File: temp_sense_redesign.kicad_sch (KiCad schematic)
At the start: 105 parts, among them IC1 TLV75533PDYDR, J1 Screw_Terminal_01x08, J2 Screw_Terminal_01x08, J3 Screw_Terminal_01x08, SW1 SW_Push, U2 AP63205, U3 MCP2517FDT-H_SL, U5 CLV4051ATDWRG4Q1, U6 CLV4051ATDWRG4Q1, U7 CLV4051ATDWRG4Q1, Y1 Crystal

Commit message: main
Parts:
- added C41: 1uF, Capacitor_SMD:C_1206_3216Metric_Pad1.33x1.80mm_HandSolder, symbol Device:C
- added C42: 1u, Capacitor_SMD:C_1206_3216Metric_Pad1.33x1.80mm_HandSolder, symbol Device:C
- added D1: Littelfuse SMF24CA, Diode_SMD:D_SOD-123F, symbol Device:D_TVS_Small
- added F1: Fuse, symbol Device:Fuse
- added IC2: LM74500QDDFRQ1, SOT65P280X110-8N, symbol custom_components:LM74500QDDFRQ1
- added J4: Conn_01x02_Pin, symbol Connector:Conn_01x02_Pin
- added J6: Screw_Terminal_01x08, symbol Connector:Screw_Terminal_01x08
- added Q1: Q_NMOS_DGS, symbol Transistor_FET:Q_NMOS_DGS
- added TP1, TP2, TP3: TestPoint, symbol Connector:TestPoint
- IC1: value TLV75533PDYDR -> TPS7A03
- U1: value ~ -> MSPM0C1104SDGS20R
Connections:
- net +3.3V: now also TP1.1
- net +5V: now also TP2.1
- net GND: now also J1.4 (Pin_4), J1.8 (Pin_8), J2.4 (Pin_4), J2.8 (Pin_8), J3.4 (Pin_4), J3.8 (Pin_8), J6.4 (Pin_4), J6.8 (Pin_8), TP3.1
- net SWCLK: now also J4.1 (Pin_1)
- net TI12: now also J6.3 (Pin_3); no longer J2.4 (Pin_4)
- net TI16: now also J6.5 (Pin_5); no longer J2.8 (Pin_8)
- net TI20: now also J6.6 (Pin_6); no longer J3.4 (Pin_4)
- net TI24: now also J6.7 (Pin_7); no longer J3.8 (Pin_8)
- net TI4: now also J6.1 (Pin_1); no longer J1.4 (Pin_4)
- net TI8: now also J6.2 (Pin_2); no longer J1.8 (Pin_8)
- net at U1.15 (PA19/SWDIO): now also J4.2 (Pin_2)
- net +12V renamed 24V
- net 24V: now also F1.2, Q1.1 (D)
- net AI4: no longer names the net of U1.12 (PA16/A8)
- net AI5: no longer names the net of U1.1 (PA26/A1)
- net UART_RX: no longer names the net of U1.3 (PA28/A5)
- net UART_TX: no longer names the net of U1.2 (PA27/A0)
- new net: C42.1, D1.2 (A2), IC2.1 (EN), Q1.3 (S)
- new net: C42.2, D1.1 (A1), IC2.2 (GND)
- new net: C41.1, IC2.4 (VCAP)
- new net: C41.2, F1.1, IC2.5 (SOURCE)
- new net gate: IC2.6 (GATE), Q1.2 (G)
- no-connect marks 3 -> 7

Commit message: final
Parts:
- removed R2: 120, symbol Device:R_Small
- removed R27, R28, R29, R30, R35, R36, R39, R40, R43, R44, R45, R46: 1M, Resistor_SMD:R_0603_1608Metric, symbol Device:R_Small
- removed R31, R32, R33, R34, R37, R38, R41, R42, R47, R48, R49, R50: 680, Resistor_SMD:R_0603_1608Metric, symbol Device:R_Small
- added C43: 1uF, Capacitor_SMD:C_0603_1608Metric, symbol Device:C_Small
- added J5: Screw_Terminal_01x02, symbol Connector:Screw_Terminal_01x02
- added J7: Conn_01x02_Pin, symbol Connector:Conn_01x02_Pin
- added R81: 1M, Resistor_SMD:R_0603_1608Metric, symbol Device:R_Small
- R10, R13, R14, R17, R18, R19, R23, R24, R3, R5, R6, R9: value 1M -> 680
- Y1: value Crystal -> HC49/4HSMX
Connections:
- net +3.3V: no longer R11.2, R12.2, R15.2, R16.2, R20.2, R21.2, R22.2, R25.2, R26.2, R4.2, R7.2, R8.2
- net +5V: now also C14.1, IC1.3 (EN)
- net 24V: no longer C1.1, U2.2 (EN), U2.3 (VIN)
- net CANL: now also J5.2 (Pin_2)
- net GND: now also C43.2, J7.2 (Pin_2)
- net T1: now also R21.1; no longer R17.2
- net T10: now also R11.1; no longer R19.2
- net T11: now also R12.1; no longer R23.2
- net T12: now also R13.1; no longer R24.2
- net T13: now also R14.1
- net T14: now also R15.1
- net T15: now also R16.1
- net T16: now also R17.1
- net T17: now also R18.1
- net T18: now also R19.1
- net T19: now also R20.1
- net T2: now also R3.1; no longer R3.2
- net T20: now also R22.1
- net T21: now also R23.1
- net T22: now also R24.1
- net T23: now also R25.1
- net T24: now also R26.1
- net T3: now also R4.1; no longer R5.2
- net T4: now also R5.1; no longer R6.2
- net T5: now also R6.1; no longer R9.2
- net T6: now also C23.1, R7.1, R7.2; no longer C22.1, R10.2
- net T7: now also C25.1, R9.1; no longer C23.1, R13.2
- net T8: now also R8.1; no longer R14.2
- net T9: now also C22.1, R10.1; no longer C25.1, R18.2
- net TI1: now also R21.2; no longer R17.1, R21.1
- net TI10: now also R11.2; no longer R19.1, R22.1
- net TI11: now also R12.2; no longer R23.1, R25.1
- net TI12: now also R13.2; no longer R24.1, R26.1
- net TI13: now also R14.2
- net TI14: now also R15.2
- net TI15: now also R16.2
- net TI16: now also R17.2
- net TI17: now also R18.2
- net TI18: now also R19.2
- net TI19: now also R20.2
- net TI2: now also R3.2; no longer R3.1, R4.1
- net TI20: now also R22.2
- net TI21: now also R23.2
- net TI22: now also R24.2
- net TI23: now also R25.2
- net TI24: now also R26.2
- net TI3: now also R4.2; no longer R5.1, R7.1
- net TI4: now also R5.2; no longer R6.1, R8.1
- net TI5: now also R6.2; no longer R11.1, R9.1
- net TI6: no longer R10.1, R12.1
- net TI7: now also R9.2; no longer R13.1, R15.1
- net TI8: now also R8.2; no longer R14.1, R16.1
- net TI9: now also R10.2; no longer R18.1, R20.1
- net at U1.1 (PA26/A1): now also R81.1
- net CAN_H renamed CANH
- net CANH: now also J5.1 (Pin_1)
- new net +24V: C1.1, U2.2 (EN), U2.3 (VIN)
- new net AOUT: C43.1, J7.1 (Pin_1), R81.2
- no-connect marks 7 -> 6
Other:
- moved on the sheet: C10, C11, C12, C14, C17, C41, C42, C8, C9, D1, F1, IC2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

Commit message: Update design files, add custom library and footprints
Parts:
- removed C10, C11: 22p, Capacitor_SMD:C_1206_3216Metric_Pad1.33x1.80mm_HandSolder, symbol Device:C
- removed C12: 0.1uF, Capacitor_SMD:C_1206_3216Metric_Pad1.33x1.80mm_HandSolder, symbol Device:C
- removed C14, C15, C41: 1uF, Capacitor_SMD:C_1206_3216Metric_Pad1.33x1.80mm_HandSolder, symbol Device:C
- removed C42: 1u, Capacitor_SMD:C_1206_3216Metric_Pad1.33x1.80mm_HandSolder, symbol Device:C
- removed C8, C9: 0.1µ, Capacitor_SMD:C_1206_3216Metric_Pad1.33x1.80mm_HandSolder, symbol Device:C
- removed R26: 680, Resistor_SMD:R_0603_1608Metric, symbol Device:R_Small
- added C10: 22p, Capacitor_SMD:C_0603_1608Metric, symbol Device:C_Small
- added C11: 10u, Capacitor_SMD:C_0603_1608Metric_Pad1.08x0.95mm_HandSolder, symbol Device:C_Small
- added C12, C8, C9: 0.1µF, Capacitor_SMD:C_0603_1608Metric, symbol Device:C_Small
- added C14, C15, C41, C42: 1uF, Capacitor_SMD:C_0603_1608Metric, symbol Device:C_Small
- added H1, H2, H3, H4: MountingHole, MountingHole:MountingHole_3.2mm_M3, symbol Mechanical:MountingHole
- added J8: Screw_Terminal_01x02, Library:1725656, symbol Connector:Screw_Terminal_01x02
- added R2: 680, Resistor_SMD:R_0603_1608Metric, symbol Device:R_Small
- C1: value 10μ -> 22uF; footprint (none) -> Capacitor_SMD:C_0603_1608Metric; Inventory (none) -> No; Mouser P/N (none) -> 963-MLASG32MSB5226MP
- C13, C16: value 1uF -> 0.1µF; Inventory (none) -> Yes; Mouser P/N (none) -> 81-GCM188R71C104KA7J
- C17, C18, C19, C20, C21, C22, C23, C24, C25, C26, C27, C28, C29, C30, C31, C32, C33, C34, C35, C36, C37, C38, C39: Inventory (none) -> No; Mouser P/N (none) -> 81-GXT155R61A474KE1D
- C2: footprint (none) -> Capacitor_SMD:C_0603_1608Metric; Mouser P/N (none) -> 810-C1608X8R1H104K
- C3: value 22μ -> 22uF; footprint (none) -> Capacitor_SMD:C_0603_1608Metric; Inventory (none) -> No; Mouser P/N (none) -> 963-MLASG32MSB5226MP
- C4: value 22μ -> 10u; footprint (none) -> Capacitor_SMD:C_0603_1608Metric; Inventory (none) -> No; Mouser P/N (none) -> 81-ZRB18AR6YA106ME1L
- C40: value 470nF -> 0.1µF; Inventory (none) -> Yes; Mouser P/N (none) -> 81-GCM188R71C104KA7J
- C43: Inventory (none) -> Yes; Mouser P/N (none) -> 81-GRM1887R1E105KA2D
- C44: value 1uF -> 22p; Inventory (none) -> No; Mouser P/N (none) -> 81-GCQ0335C1H220JB1D
- C5: value 10µ -> 470nF; footprint (none) -> Capacitor_SMD:C_0603_1608Metric; Inventory (none) -> No; Mouser P/N (none) -> 81-GXT155R61A474KE1D
- C6: value 0.1µ -> 0.1µF; footprint (none) -> Capacitor_SMD:C_0603_1608Metric; Inventory (none) -> Yes; Mouser P/N (none) -> 81-GCM188R71C104KA7J
- C7: value 100µ -> 10n; footprint (none) -> Capacitor_SMD:C_0603_1608Metric; Inventory (none) -> Yes; Mouser P/N (none) -> 603-CC0603JR7R7BB103
- D1: Inventory (none) -> No; Mouser P/N (none) -> 576-SMF24CA
- F1: value Fuse -> 3568; footprint (none) -> Fuse:Fuseholder_Blade_Mini_Keystone_3568; Inventory (none) -> Yes; Mouser P/N (none) -> 534-3568
- IC2: footprint SOT65P280X110-8N -> Package_TO_SOT_SMD:TSOT-23-8_HandSoldering; Arrow Part Number LM74500QDDFRQ1 -> (none); Arrow Price/Stock null?region=nac -> (none); Height 1.1 -> (none); Manufacturer_Name Texas Instruments -> (none); Manufacturer_Part_Number LM74500QDDFRQ1 -> (none); Mouser P/N (none) -> 595-LM74500QDDFRQ1; Mouser Part Number 595-LM74500QDDFRQ1 -> (none); Mouser Price/Stock https://www.mouser.co.uk/ProductDetail/Texas-Instruments/LM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 -> (none)
- J1, J2, J3, J6: footprint (none) -> Library:1725711; Inventory (none) -> No; Mouser P/N (none) -> 490-TB003-500-P03BE
- J4, J7: footprint (none) -> Connector_PinSocket_2.00mm:PinSocket_1x02_P2.00mm_Vertical
- J5: footprint (none) -> Library:1725656; Inventory (none) -> No; Mouser P/N (none) -> 651-1725656
- L1: footprint (none) -> Library:inductorcustome27; Inventory (none) -> No; Mouser P/N (none) -> 70-IHLP2020BZR4R7M1A
- Q1: value Q_NMOS_DGS -> SUD20N10-66L-GE3; footprint (none) -> Library:SUD20N1066LGE3; Inventory (none) -> No; Mouser P/N (none) -> 78-SUD20N10-66L-GE3
- R1: footprint (none) -> Resistor_SMD:R_0603_1608Metric; Inventory (none) -> No; Mouser P/N (none) -> 652-CR1206FX-4752ELF
- R10, R11, R12, R13, R14, R15, R16, R17, R18, R19, R20, R21, R22, R23, R24, R25, R3, R4, R5, R6, R7, R8, R9: Inventory (none) -> Yes; Mouser P/N (none) -> 667-ERJ-3EKF6800V
- R81: Inventory (none) -> Yes; Mouser P/N (none) -> 667-ERJ-3EKF1004V
- SW1: footprint (none) -> Library:KSC251JSPDELTALFS; Inventory (none) -> No; Mouser P/N (none) -> 611-KSC251JSPDELTALF
- TP1, TP2, TP3: footprint (none) -> TestPoint:TestPoint_Pad_1.5x1.5mm
- U1: footprint (none) -> Library:MSPMOC; Mouser P/N (none) -> 595-MSPM0C1104SDG20R
- U2: Inventory (none) -> No; Mouser P/N (none) -> 621-AP63205WU-7
- U3: footprint (none) -> Package_SO:SOIC-14_3.9x8.7mm_P1.27mm; Mouser P/N (none) -> 579-MCP2517FD-H/SL
- U4: value ~ -> MCP2517FD-H/SL; footprint (none) -> Package_TO_SOT_SMD:Texas_DDF0008A_SOT-8_1.6x2.9mm_P0.65mm; Mouser P/N (none) -> 595-TCAN1057AVDDFRQ1
- U5, U6, U7: Mouser P/N (none) -> 595-CLV4051ATDWRG4Q1
- Y1: footprint (none) -> Library:830017146; Inventory (none) -> No; Mouser P/N (none) -> 710-830017146
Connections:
- net +3.3V: now also C13.2, C16.2, C4.1, C40.2, C6.2, R1.2, U1.6 (VDD), U4.5 (VIO), C12.1, C15.1, C8.2; no longer C13.1, C16.1, C44.1, U4.8 (VIO)
- net +5V: now also C1.1, C14.2, C9.2; no longer C4.1
- net AI2: no longer U7.3 (X)
- net AI3: now also U7.3 (X)
- net CANH: now also J5.2 (Pin_2), U4.7 (CANH); no longer J5.1 (Pin_1), U4.6 (CANH)
- net CANL: now also J5.1 (Pin_1), U4.6 (CANL); no longer J5.2 (Pin_2), U4.7 (CANL)
- net GND: now also C13.1, C16.1, C40.1, C44.1, C5.2, J3.1 (Pin_1), J3.5 (Pin_5), J6.1 (Pin_1), J6.5 (Pin_5), U4.8 (S), C10.1, C11.1, C12.2, C14.1, C15.2, C8.1, C9.1, J8.2 (Pin_2); no longer C13.2, C16.2, C40.2, C44.2, C5.1, J3.4 (Pin_4), J3.8 (Pin_8), J6.4 (Pin_4), J6.8 (Pin_8), U4.5 (S)
- net T16: now also R9.1; no longer R17.1
- net T17: now also C22.1, R17.1; no longer C33.1, R18.1
- net T18: now also C33.1, R18.1; no longer C34.1, R19.1
- net T19: now also C34.1, R19.1; no longer C35.1, R20.1
- net T2: now also R2.1; no longer R3.1
- net T20: now also C35.1, R20.1; no longer C36.1, R22.1
- net T21: now also C36.1, R22.1; no longer C37.1, R23.1
- net T22: now also C37.1, R23.1; no longer C38.1, R24.1
- net T23: now also C38.1, R24.1; no longer C39.1, R25.1
- net T24: now also C39.1, R25.1; no longer C40.1
- net T3: now also R3.1; no longer R4.1
- net T4: now also R4.1; no longer R5.1
- net T5: now also R5.1; no longer R6.1
- net T6: now also R6.1; no longer R7.1, R7.2
- net T7: now also R8.1; no longer R9.1
- net T8: now also R7.1; no longer R8.1
- net T9: now also C5.1; no longer C22.1
- net TI1: now also J3.6 (Pin_6); no longer J1.1 (Pin_1)
- net TI10: now also J3.2 (Pin_2); no longer J2.2 (Pin_2)
- net TI11: now also J3.3 (Pin_3); no longer J2.3 (Pin_3)
- net TI12: now also J6.7 (Pin_7); no longer J6.3 (Pin_3)
- net TI13: now also J1.6 (Pin_6); no longer J2.5 (Pin_5)
- net TI14: now also J2.2 (Pin_2); no longer J2.6 (Pin_6)
- net TI15: now also J1.7 (Pin_7); no longer J2.7 (Pin_7)
- net TI16: now also J2.1 (Pin_1), R9.2; no longer J6.5 (Pin_5), R17.2
- net TI17: now also J6.3 (Pin_3), R17.2; no longer J3.1 (Pin_1), R18.2
- net TI18: now also J6.4 (Pin_4), R18.2; no longer J3.2 (Pin_2), R19.2
- net TI19: now also J6.6 (Pin_6), R19.2; no longer J3.3 (Pin_3), R20.2
- net TI2: now also J3.7 (Pin_7), R2.2; no longer J1.2 (Pin_2), R3.2
- net TI20: now also J6.2 (Pin_2), R20.2; no longer J6.6 (Pin_6), R22.2
- net TI21: now also J2.3 (Pin_3), R22.2; no longer J3.5 (Pin_5), R23.2
- net TI22: now also J2.7 (Pin_7), R23.2; no longer J3.6 (Pin_6), R24.2
- net TI23: now also J2.5 (Pin_5), R24.2; no longer J3.7 (Pin_7), R25.2
- net TI24: now also J2.6 (Pin_6), R25.2; no longer J6.7 (Pin_7)
- net TI3: now also J3.8 (Pin_8), R3.2; no longer J1.3 (Pin_3), R4.2
- net TI4: now also J3.4 (Pin_4), R4.2; no longer J6.1 (Pin_1), R5.2
- net TI5: now also J1.1 (Pin_1), R5.2; no longer J1.5 (Pin_5), R6.2
- net TI6: now also J1.5 (Pin_5), R6.2; no longer J1.6 (Pin_6)
- net TI7: now also J1.2 (Pin_2), R8.2; no longer J1.7 (Pin_7), R9.2
- net TI8: now also J1.3 (Pin_3), R7.2; no longer J6.2 (Pin_2), R8.2
- net TI9: now also J6.8 (Pin_8); no longer J2.1 (Pin_1)
- net at U3.6 (OSC1), Y1.1: now also C44.2
- net 24_bat: now reaches D1.2 (A2), IC2.1 (EN), Q1.3 (S)
- net 24_bat: now also F1.1, IC2.5 (SOURCE), C41.2, C42.1
- net at D1.1 (A1), IC2.2 (GND): now also C42.2
- net at IC2.4 (VCAP): now also C41.1
- net SWDIO: now reaches J4.2 (Pin_2), U1.15 (PA19/SWDIO)
- net at U3.5 (OSC2), Y1.2: now also C10.2
- net +24V renamed vbat_output
- net vbat_output: now also Q1.1 (D), C11.2; no longer C1.1
- removed net +3V3: C5.2, C6.2, R1.2, U1.6 (VDD)
- net 24V: no longer names the net of F1.2
- net 24V: now also J8.1 (Pin_1); no longer Q1.1 (D)
- no-connect marks 6 -> 9
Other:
- moved on the sheet: D1, F1, IC2, J1, J4, J5, J7, Q1, TP1, TP2, TP3, U3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

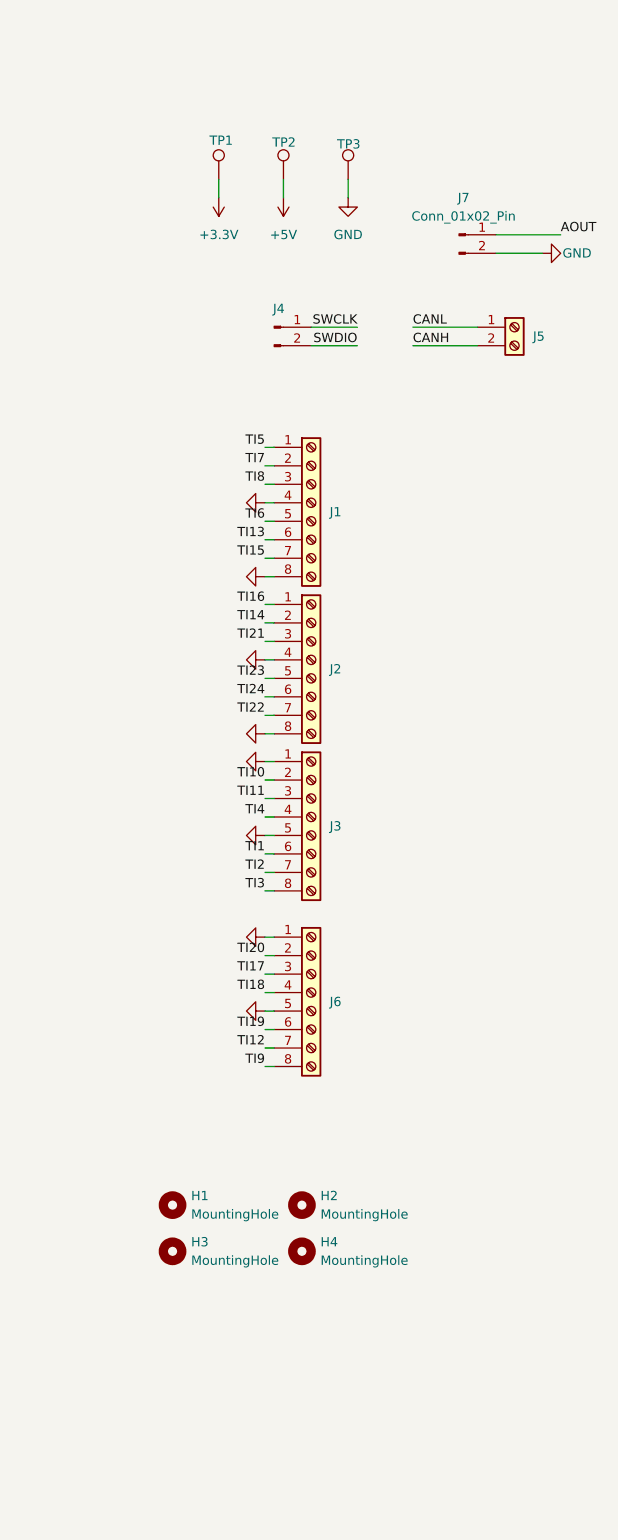
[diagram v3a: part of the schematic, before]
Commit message: Add KiCad .gitignore, remove gerber/backup/cache files from tracking
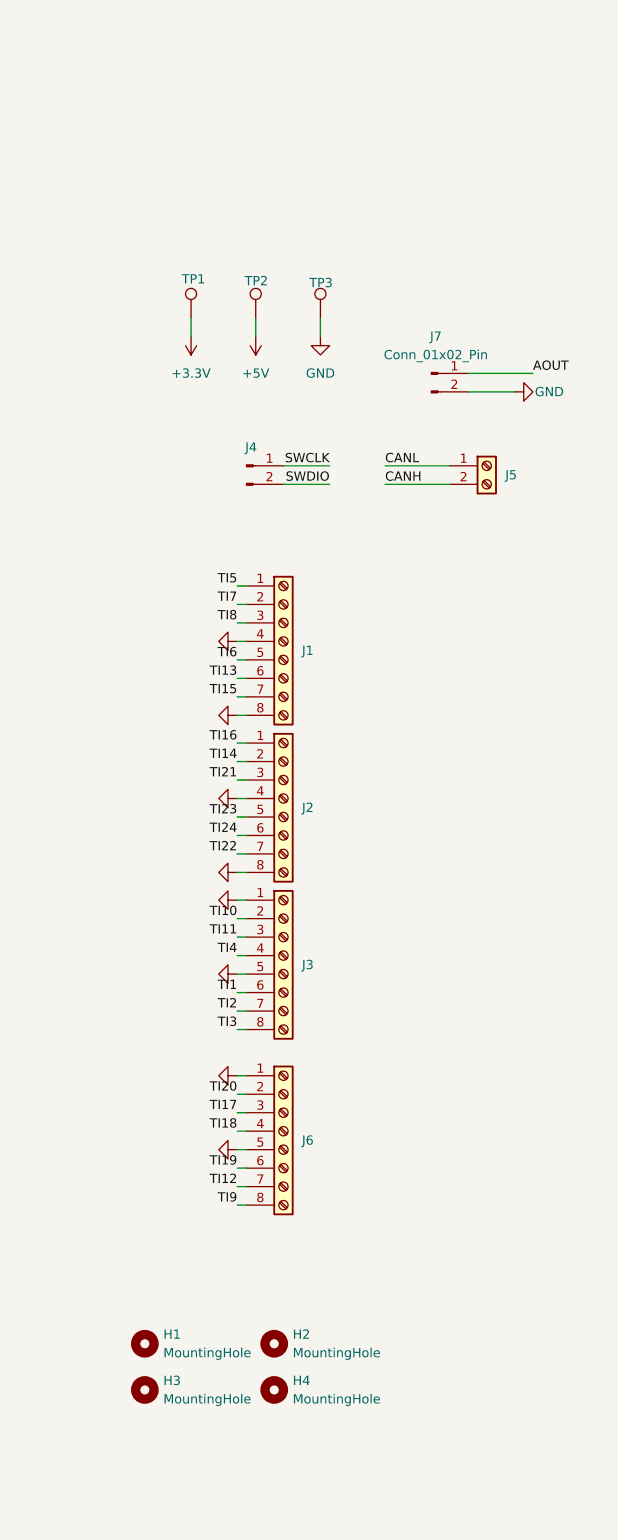
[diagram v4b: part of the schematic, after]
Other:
- moved on the sheet: H1, H2, H3, H4, J1, J2, J3, J4, J5, J6, J7, TP1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
